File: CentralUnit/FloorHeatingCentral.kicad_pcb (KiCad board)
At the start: 2 copper layers, 100 x 100 mm, 118 parts, among them J1 Conn_01x02, J10 Conn_01x02, J11 Conn_01x02, J12 Conn_01x02, J13 Conn_01x02, J14 Conn_01x02, J15 Conn_01x03, J16 Conn_01x03, J17 Conn_01x03, J18 Conn_01x03, J19 Conn_01x03, J2 Conn_01x03, J20 Conn_01x03, J21 Conn_01x03, J22 Conn_01x03, J23 Conn_01x03, J24 Conn_01x03, J25 Conn_02x05_Odd_Even, J26 Conn_01x02, J3 Conn_01x20, J4 Conn_01x06, J5 Conn_01x02, J6 Conn_01x02, J7 Conn_01x02, J8 Conn_01x02, J9 Conn_01x02, Q1 Q_NMOS_GDS, Q10 Q_NMOS_GDS, Q2 Q_NMOS_GDS, Q3 Q_NMOS_GDS, Q4 Q_NMOS_GDS, Q5 Q_NMOS_GDS, Q6 Q_NMOS_GDS, Q7 Q_NMOS_GDS, Q8 Q_NMOS_GDS, Q9 Q_NMOS_GDS, U1 ESP32-WROOM, U10 LM1117-3.3, U2 ISO1540DR, U3 ISO1540DR, U4 ISO1540DR, U5 ISO1540DR, U6 ISO1540DR, U7 74HC595D_118, U8 74HC595D_118, U9 MP1584

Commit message: Added alternative resistor to connect LCD brightness to DAC
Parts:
- added R51: R, Resistors_SMD:R_0603, F.Cu at (169.5, 126.5)
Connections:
- net /ActuatorConn/GATE renamed /GATE_3
- net /sheet5C0162C8/GATE renamed /GATE_9
- net /sheet5C0163D9/GATE renamed /GATE
- net /sheet5C0163DC/GATE renamed /GATE_8
- net /sheet5C016537/GATE renamed /GATE_7
- net /sheet5C01653A/GATE renamed /GATE_6
- net /sheet5C01653D/GATE renamed /GATE_5
- net /sheet5C016540/GATE renamed /GATE_4
- net /sheet5C0169FB/GATE renamed /GATE_2
- net /sheet5C0169FE/GATE renamed /GATE_1
- net Net-(R3-Pad2) renamed /TXD
- net Net-(R4-Pad2) renamed /RXD
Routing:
- net /IO0: track 34.2 -> 92.1 mm
- net Net-(J3-Pad3): track 6.59 -> 21.3 mm, vias 0 -> 1

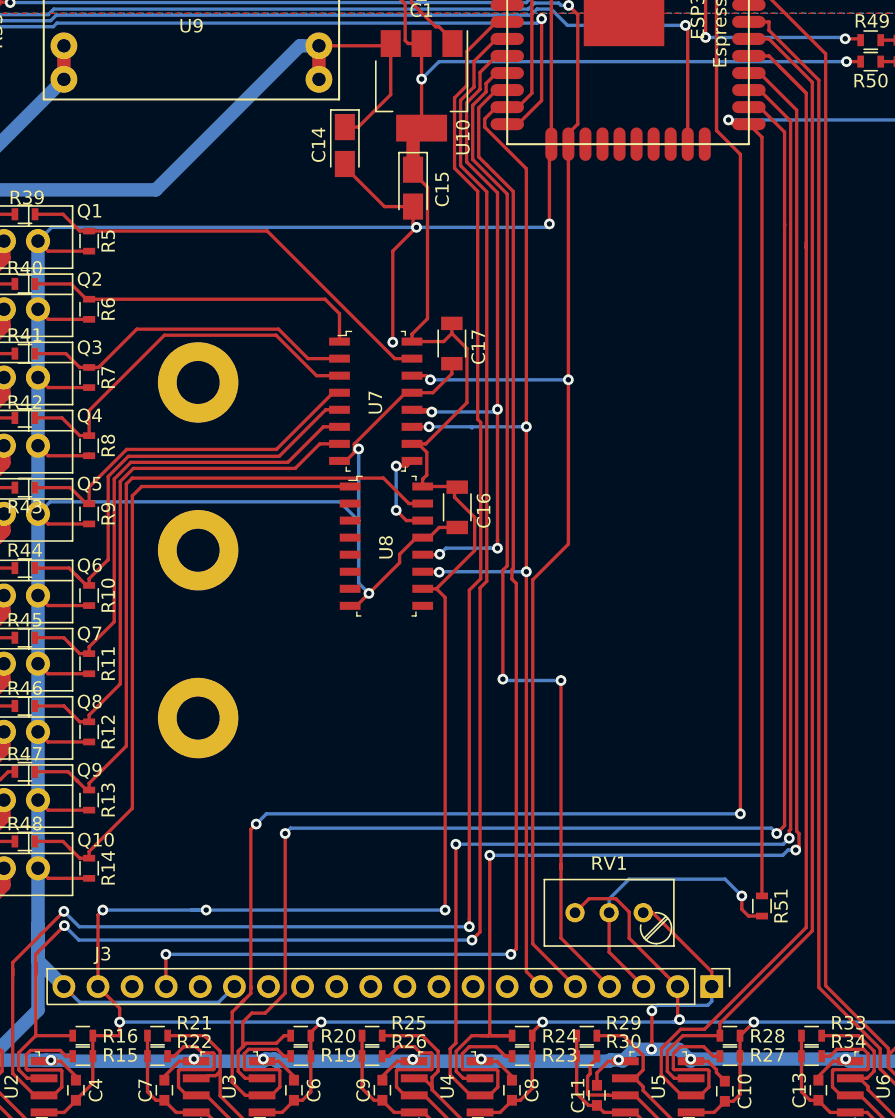
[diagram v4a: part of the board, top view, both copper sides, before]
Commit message: Added possibility to PWM LCD light and updated README
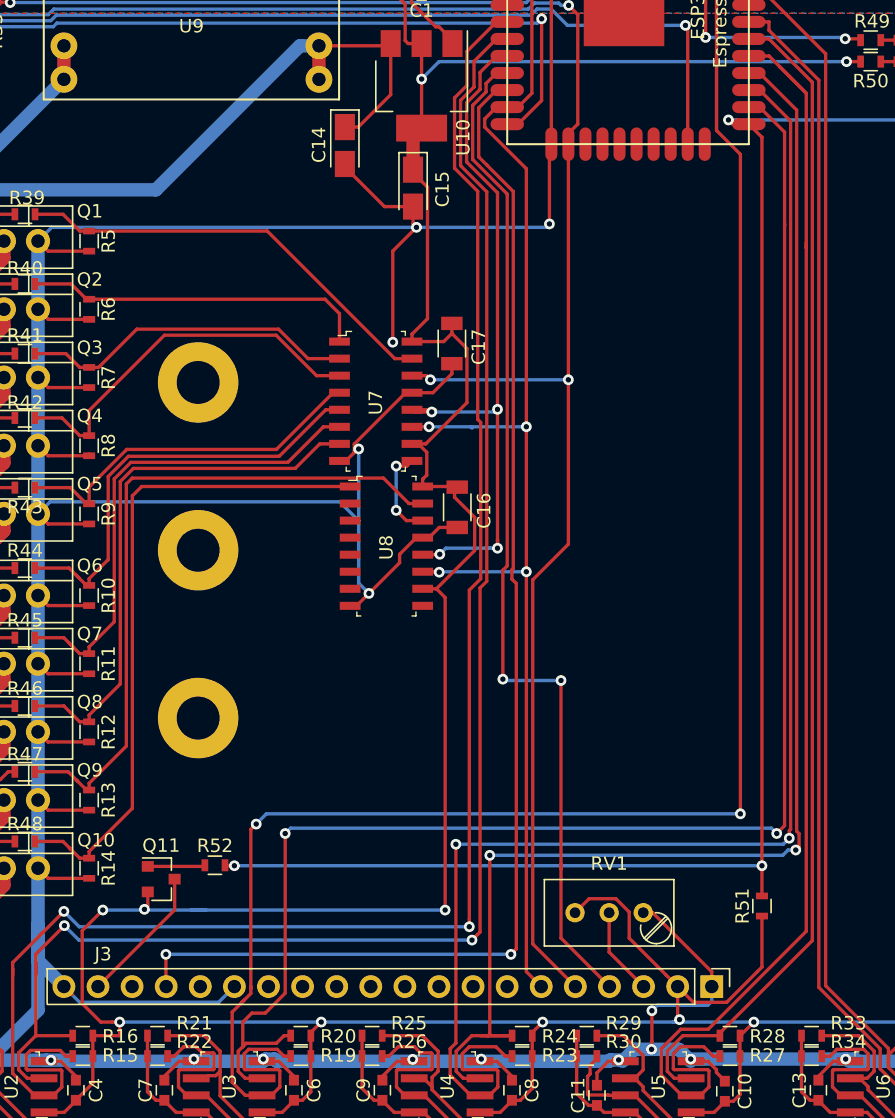
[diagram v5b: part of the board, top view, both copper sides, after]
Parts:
- added Q11: Q_PMOS_GSD, TO_SOT_Packages_SMD:SOT-23, F.Cu at (124.8, 124.5)
- added R52: 330, Resistors_SMD:R_0603, F.Cu at (128.8, 123.5)
- R51: value R -> Inf
- turned R51 to 90 degrees
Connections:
- J3 pad 19: +3V3 -> /VDD_DL
- R51 pad 1: /IO0 -> +3V3
- R51 pad 2: Net-(J3-Pad3) -> /IO0
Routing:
- net /IO0: track 92.1 -> 132.1 mm, vias 1 -> 3
- net +3V3: track 331.7 -> 346.5 mm
- net Net-(J3-Pad3): track 21.3 -> 6.59 mm, vias 1 -> 0
- net /VDD_DL: track 0.00 -> 10.4 mm
- net Net-(Q11-Pad1): track 0.00 -> 4.29 mm

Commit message: Major work changing over to 868MHz solution. Current state unfinished
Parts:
- removed C10, C11, C12, C13, C5, C6, C7, C8, C9: 0.1u, Capacitors_SMD:C_0603
- removed C14, C15: 10u, Capacitors_Tantalum_SMD:CP_Tantalum_Case-A_EIA-3216-18_Reflow
- removed C16, C17: 0.1u, Capacitors_SMD:C_1206
- removed D2: LED, LEDs:LED_0603
- removed J14: Conn_01x02, parts:ScrewTerminal_2x2.54
- removed J15, J16, J17, J18, J19, J20, J21, J22, J23, J24: Conn_01x03, parts:ScrewTerminal_3x2.54
- removed J25: Conn_02x05_Odd_Even, Pin_Headers:Pin_Header_Straight_2x05_Pitch2.54mm
- removed J26: Conn_01x02, Pin_Headers:Pin_Header_Straight_1x02_Pitch2.54mm
- removed R28, R31, R32: 2.7K, Resistors_SMD:R_0603
- removed R29, R30, R33, R34: 300R, Resistors_SMD:R_0603
- removed R35, R36, R37, R38: 100R, Resistors_SMD:R_0603
- removed R39, R40, R41, R42, R43, R44, R45, R46, R47, R48: 560R, Resistors_SMD:R_0603
- removed R49, R50: 660R, Resistors_SMD:R_0603
- removed R51: Inf, Resistors_SMD:R_0603
- removed R52: 330, Resistors_SMD:R_0603
- removed U10: LM1117-3.3, TO_SOT_Packages_SMD:SOT-223-3_TabPin2
- removed U7, U8: 74HC595D_118, digikey-footprints:SOIC-16_W3.90mm
- removed U9: MP1584, mp1584:MP1584
- added JP1: Jumper_2_Open, TestPoint:TestPoint_2Pads_Pitch2.54mm_Drill0.8mm, F.Cu at (96.0, 109.5)
- C1: footprint Capacitors_SMD:C_0603 -> Capacitor_SMD:C_1206_3216Metric
- C2: value 10u -> 0.1u; footprint Capacitors_Tantalum_SMD:CP_Tantalum_Case-A_EIA-3216-18_Reflow -> Capacitor_SMD:C_1206_3216Metric
- C3, C4: value 0.1u -> 10u; footprint Capacitors_SMD:C_0603 -> Capacitor_Tantalum_SMD:CP_EIA-3216-18_Kemet-A
- D1: footprint LEDs:LED_0603 -> LED_SMD:LED_0603_1608Metric
- H1, H2: moved to F.Cu
- J1: value Conn_01x02 -> Screw_Terminal_01x02; footprint Pin_Headers:Pin_Header_Straight_1x02_Pitch2.54mm -> TerminalBlock_Phoenix:TerminalBlock_Phoenix_MKDS-3-2-5.08_1x02_P5.08mm_Horizontal
- J10, J11, J12, J13, J5, J6, J7, J8, J9: value Conn_01x02 -> Screw_Terminal_01x02; footprint parts:ScrewTerminal_2x2.54 -> TerminalBlock_Phoenix:TerminalBlock_Phoenix_MKDS-3-2-5.08_1x02_P5.08mm_Horizontal
- J2: value Conn_01x03 -> Conn_02x05_Odd_Even; footprint Pin_Headers:Pin_Header_Straight_1x03_Pitch2.54mm -> Connector_IDC:IDC-Header_2x05_P2.54mm_Vertical
- J4: value Conn_01x06 -> Screw_Terminal_01x02; footprint Pin_Headers:Pin_Header_Straight_1x06_Pitch2.54mm -> TerminalBlock_Phoenix:TerminalBlock_Phoenix_MKDS-3-2-5.08_1x02_P5.08mm_Horizontal
- Q1, Q10, Q2, Q3, Q4, Q5, Q6, Q7, Q8, Q9: footprint TO_SOT_Packages_THT:TO-220-3_Vertical -> Package_TO_SOT_THT:TO-220-3_Vertical
- Q11: value Q_PMOS_GSD -> Q_NMOS_GDS; footprint TO_SOT_Packages_SMD:SOT-23 -> Package_TO_SOT_THT:TO-220-3_Vertical
- R1, R11, R13, R9: footprint Resistors_SMD:R_0603 -> Resistor_SMD:R_1206_3216Metric
- R10, R12, R14, R8: value 10K -> 560R; footprint Resistors_SMD:R_0603 -> Resistor_SMD:R_1206_3216Metric
- R15, R19, R23, R27: value 2.7K -> 10K; footprint Resistors_SMD:R_0603 -> Resistor_SMD:R_1206_3216Metric
- R16, R20, R24: value 2.7K -> 560R; footprint Resistors_SMD:R_0603 -> Resistor_SMD:R_1206_3216Metric
- R17, R21, R25: value 300R -> 10K; footprint Resistors_SMD:R_0603 -> Resistor_SMD:R_1206_3216Metric
- R18, R22, R26: value 300R -> 560R; footprint Resistors_SMD:R_0603 -> Resistor_SMD:R_1206_3216Metric
- R2: value 4.7K -> 560R; footprint Resistors_SMD:R_0603 -> Resistor_SMD:R_1206_3216Metric
- R3, R4: value 470R -> 100R; footprint Resistors_SMD:R_0603 -> Resistor_SMD:R_0201_0603Metric
- R5, R7: value 10K -> 100R; footprint Resistors_SMD:R_0603 -> Resistor_SMD:R_0201_0603Metric
- R6: value 10K -> 660R; footprint Resistors_SMD:R_0603 -> Resistor_SMD:R_1206_3216Metric
- RV1: footprint Potentiometers:Potentiometer_Trimmer_Bourns_3296W -> Potentiometer_SMD:Potentiometer_Bourns_3269W_Vertical
- U1: value ESP32-WROOM -> ESP32-DevKitC; footprint ESP32-footprints-Lib:ESP32-WROOM -> Espressif:ESP32-DevKitC
- U2, U3: value ISO1540DR -> 74HC595D_118; footprint digikey-footprints:SOIC-8_W3.9mm -> digikey-footprints:SOIC-16_W3.90mm
- U4: value ISO1540DR -> RFM69-ATSHA-breakout; footprint digikey-footprints:SOIC-8_W3.9mm -> RFM69HCW_ATSHA204A_Breakout:RFM69HCW_ATSHA204A_Breakout
- U5: value ISO1540DR -> MP1584; footprint digikey-footprints:SOIC-8_W3.9mm -> mp1584:MP1584
- U6: value ISO1540DR -> LM1117-5.0; footprint digikey-footprints:SOIC-8_W3.9mm -> Package_TO_SOT_SMD:SOT-223-3_TabPin2
- moved H1 284.1 mm to (388.4, 212.4)
- moved H2 237.8 mm to (399.6, 212.4)
- moved J4 140.6 mm to (96.3, 164.1), turned to 0 degrees
- moved R2 117.4 mm to (111.8, 132.1)
- moved J2 116.1 mm to (93.5, 117.5), turned to 0 degrees
- moved R4 108.0 mm to (100.6, 120.4), turned to 180 degrees
- moved R3 104.5 mm to (100.6, 117.9), turned to 180 degrees
- moved J1 101.5 mm to (96.5, 92.1), turned to 90 degrees
- moved J13 95.1 mm to (187.7, 164.1), turned to 0 degrees
- moved J12 89.1 mm to (177.6, 164.1), turned to 0 degrees
- moved D1 87.7 mm to (94.0, 76.5), turned to 0 degrees
- moved J5 87.1 mm to (106.4, 164.1), turned to 0 degrees
- moved R1 86.7 mm to (111.8, 137.2), turned to -90 degrees
- moved J11 84.2 mm to (167.4, 164.1), turned to 0 degrees
- moved J6 83.0 mm to (116.6, 164.1), turned to 0 degrees
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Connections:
- C1 pad 1: Net-(C1-Pad1) -> GND
- C1 pad 2: GND -> +3V3
- C2 pad 1: +3V3 -> GND
- C2 pad 2: GND -> +3V3
- C3 pad 1: +3V3 -> +7.5V
- C4 pad 1: +3V3 -> +5V
- J1 pad 1: Net-(C1-Pad1) -> +24V
- J10 pad 1: Net-(J10-Pad1) -> /sheet5C01653D/ValSW
- J11 pad 1: Net-(J11-Pad1) -> /sheet5C016540/ValSW
- J12 pad 1: Net-(J12-Pad1) -> /sheet5C0169FB/ValSW
- J13 pad 1: Net-(J13-Pad1) -> /sheet5C0169FE/ValSW
- J2 pad 1: (no net) -> Net-(J2-Pad1)
- J2 pad 2: /IO0 -> Net-(J2-Pad2)
- J2 pad 3: Net-(J2-Pad3) -> GND
- J3 pad 10: (no net) -> unconnected-(J3-Pad10)
- J3 pad 11: (no net) -> unconnected-(J3-Pad11)
- J3 pad 12: (no net) -> unconnected-(J3-Pad12)
- J3 pad 13: (no net) -> unconnected-(J3-Pad13)
- J3 pad 14: (no net) -> unconnected-(J3-Pad14)
- J3 pad 16: (no net) -> unconnected-(J3-Pad16)
- J3 pad 18: (no net) -> unconnected-(J3-Pad18)
- J3 pad 19: /VDD_DL -> +3V3
- J3 pad 20: GND -> /GND_DL_SW
- J3 pad 5: /HSPI_MOSI_IO13 -> /VSPI_MOSI
- J3 pad 6: /HSPI_CLK_IO14 -> /VSPI_CLK
- J3 pad 7: (no net) -> unconnected-(J3-Pad7)
- J3 pad 8: (no net) -> unconnected-(J3-Pad8)
- J3 pad 9: (no net) -> unconnected-(J3-Pad9)
- J4 pad 1: GND -> /ActuatorConn/ValSW
- J4 pad 2: Net-(J4-Pad2) -> +24V
- J5 pad 1: Net-(J5-Pad1) -> /sheet5C0162C8/ValSW
- J6 pad 1: Net-(J6-Pad1) -> /sheet5C0163D9/ValSW
- J7 pad 1: Net-(J7-Pad1) -> /sheet5C0163DC/ValSW
- J8 pad 1: Net-(J8-Pad1) -> /sheet5C016537/ValSW
- J9 pad 1: Net-(J9-Pad1) -> /sheet5C01653A/ValSW
- Q1 pad 2: Net-(J5-Pad1) -> /GND_DL_SW
- Q10 pad 2: Net-(J14-Pad1) -> /sheet5C0169FB/ValSW
- Q11 pad 2: +3V3 -> /sheet5C0169FE/ValSW
- Q11 pad 3: /VDD_DL -> GND
- Q2 pad 2: Net-(J6-Pad1) -> /ActuatorConn/ValSW
- Q3 pad 2: Net-(J7-Pad1) -> /sheet5C0162C8/ValSW
- Q4 pad 2: Net-(J8-Pad1) -> /sheet5C0163D9/ValSW
- Q5 pad 2: Net-(J9-Pad1) -> /sheet5C0163DC/ValSW
- Q6 pad 2: Net-(J10-Pad1) -> /sheet5C016537/ValSW
- Q7 pad 2: Net-(J11-Pad1) -> /sheet5C01653A/ValSW
- Q8 pad 2: Net-(J12-Pad1) -> /sheet5C01653D/ValSW
- Q9 pad 2: Net-(J13-Pad1) -> /sheet5C016540/ValSW
- R1 pad 1: Net-(C1-Pad1) -> /DL_SW
- R1 pad 2: +3V3 -> GND
- R10 pad 1: /GATE_6 -> /sheet5C0162C8/GATE
- R10 pad 2: GND -> Net-(Q3-Pad1)
- R11 pad 1: /GATE_5 -> /sheet5C0162C8/GATE
- R12 pad 1: /GATE_4 -> /sheet5C0163D9/GATE
- R12 pad 2: GND -> Net-(Q4-Pad1)
- R13 pad 1: /GATE_2 -> /sheet5C0163D9/GATE
- R14 pad 1: /GATE_1 -> /sheet5C0163DC/GATE
- R14 pad 2: GND -> Net-(Q5-Pad1)
- R15 pad 1: +3V3 -> /sheet5C0163DC/GATE
- R15 pad 2: /INP0 -> GND
- R16 pad 1: /INP1 -> /sheet5C016537/GATE
- R16 pad 2: +3V3 -> Net-(Q6-Pad1)
- R17 pad 1: +5V -> /sheet5C016537/GATE
- R17 pad 2: Net-(J15-Pad3) -> GND
- R18 pad 1: Net-(J16-Pad3) -> /sheet5C01653A/GATE
- R18 pad 2: +5V -> Net-(Q7-Pad1)
- R19 pad 1: +3V3 -> /sheet5C01653A/GATE
- R19 pad 2: /INP2 -> GND
- R2 pad 1: GND -> /DL_SW
- R2 pad 2: Net-(J2-Pad3) -> Net-(Q1-Pad1)
- R20 pad 1: /INP3 -> /sheet5C01653D/GATE
- R20 pad 2: +3V3 -> Net-(Q8-Pad1)
- R21 pad 1: +5V -> /sheet5C01653D/GATE
- R21 pad 2: Net-(J17-Pad3) -> GND
- R22 pad 1: Net-(J18-Pad3) -> /sheet5C016540/GATE
- R22 pad 2: +5V -> Net-(Q9-Pad1)
- R23 pad 1: +3V3 -> /sheet5C016540/GATE
- R23 pad 2: /INP4 -> GND
- R24 pad 1: /INP5 -> /sheet5C0169FB/GATE
- R24 pad 2: +3V3 -> Net-(Q10-Pad1)
- R25 pad 1: +5V -> /sheet5C0169FB/GATE
- R25 pad 2: Net-(J19-Pad3) -> GND
- R26 pad 1: Net-(J20-Pad3) -> /sheet5C0169FE/GATE
- R26 pad 2: +5V -> Net-(Q11-Pad1)
- R27 pad 1: +3V3 -> /sheet5C0169FE/GATE
- R27 pad 2: /INP6 -> GND
- R3 pad 1: Net-(J4-Pad2) -> /TMS
- R3 pad 2: /TXD -> Net-(J2-Pad2)
- R4 pad 1: Net-(J4-Pad3) -> /TCK
- R4 pad 2: /RXD -> Net-(J2-Pad4)
- R5 pad 1: /GATE_3 -> /TDO
- R5 pad 2: GND -> Net-(J2-Pad6)
- R6 pad 1: /GATE_9 -> Net-(D1-Pad2)
- R6 pad 2: GND -> /LED
- R7 pad 1: /GATE -> /TDI
- R7 pad 2: GND -> Net-(J2-Pad8)
- R8 pad 1: /GATE_8 -> /ActuatorConn/GATE
- R8 pad 2: GND -> Net-(Q2-Pad1)
- R9 pad 1: /GATE_7 -> /ActuatorConn/GATE
- U1 pad 1: GND -> +3V3
- U1 pad 10: /SR_LATCH -> /DISP_CS
- U1 pad 11: /DISP_CS -> /DISP_RST
- U1 pad 12: /DISP_RST -> /TMS
- U1 pad 13: /HSPI_CLK_IO14 -> /TDI
- U1 pad 14: /HSPI_MISO_IO12 -> GND
- U1 pad 15: GND -> /TCK
- U1 pad 16: /HSPI_MOSI_IO13 -> unconnected-(U1-Pad16)
- U1 pad 17: (no net) -> unconnected-(U1-Pad17)
- U1 pad 18: (no net) -> unconnected-(U1-Pad18)
- U1 pad 19: (no net) -> +5V
- U1 pad 2: +3V3 -> unconnected-(U1-Pad2)
- U1 pad 20: (no net) -> unconnected-(U1-Pad20)
- U1 pad 21: (no net) -> unconnected-(U1-Pad21)
- U1 pad 22: (no net) -> unconnected-(U1-Pad22)
- U1 pad 23: /HSPI_CS0_IO15 -> /TDO
- U1 pad 24: (no net) -> unconnected-(U1-Pad24)
- U1 pad 25: /IO0 -> unconnected-(U1-Pad25)
- U1 pad 26: /INP3 -> /DL_SW
- U1 pad 27: /INP4 -> /RFM69_IRQ
- U1 pad 28: /INP5 -> /RFM69_RST
- U1 pad 29: /INP6 -> /RFM69_CS
- U1 pad 3: Net-(C1-Pad1) -> unconnected-(U1-Pad3)
- U1 pad 30: /INP7 -> /VSPI_SCK
- U1 pad 31: /INP8 -> /VSPI_MISO
- U1 pad 32: (no net) -> GND
- U1 pad 33: /INP9 -> unconnected-(U1-Pad33)
- U1 pad 34: /RXD -> unconnected-(U1-Pad34)
- U1 pad 35: /TXD -> unconnected-(U1-Pad35)
- U1 pad 36: /INP2 -> unconnected-(U1-Pad36)
- U1 pad 37: /LED -> /VSPI_MOSI
- U1 pad 4: (no net) -> unconnected-(U1-Pad4)
- U1 pad 5: (no net) -> unconnected-(U1-Pad5)
- U1 pad 6: (no net) -> unconnected-(U1-Pad6)
- U1 pad 7: (no net) -> /LED
- U1 pad 8: /INP0 -> unconnected-(U1-Pad8)
- U1 pad 9: /INP1 -> /SR_LATCH
- U2 pad 1: +3V3 -> /sheet5C0162C8/GATE
- U2 pad 2: /INP0 -> /sheet5C0163D9/GATE
- U2 pad 3: /INP1 -> /sheet5C0163DC/GATE
- U2 pad 4: GND -> /sheet5C016537/GATE
- U2 pad 5: GND -> /sheet5C01653A/GATE
- U2 pad 6: Net-(J16-Pad3) -> /sheet5C01653D/GATE
- U2 pad 7: Net-(J15-Pad3) -> /sheet5C016540/GATE
- U2 pad 8: +5V -> GND
- U3 pad 1: +3V3 -> /sheet5C0169FE/GATE
- U3 pad 2: /INP2 -> unconnected-(U3-Pad2)
- U3 pad 3: /INP3 -> unconnected-(U3-Pad3)
- U3 pad 4: GND -> unconnected-(U3-Pad4)
- U3 pad 5: GND -> unconnected-(U3-Pad5)
- U3 pad 6: Net-(J18-Pad3) -> unconnected-(U3-Pad6)
- U3 pad 7: Net-(J17-Pad3) -> unconnected-(U3-Pad7)
- U3 pad 8: +5V -> GND
- U4 pad 1: +3V3 -> /RFM69_RST
- U4 pad 2: /INP4 -> /RFM69_IRQ
- U4 pad 3: /INP5 -> unconnected-(U4-Pad3)
- U4 pad 4: GND -> unconnected-(U4-Pad4)
- U4 pad 5: GND -> unconnected-(U4-Pad5)
- U4 pad 6: Net-(J20-Pad3) -> unconnected-(U4-Pad6)
- U4 pad 7: Net-(J19-Pad3) -> unconnected-(U4-Pad7)
- U4 pad 8: +5V -> +3V3
- U5 pad 1: +3V3 -> +24V
- U5 pad 2: /INP6 -> GND
- U5 pad 3: /INP7 -> +7.5V
- U6 pad 1: +3V3 -> GND
- U6 pad 2: /INP8 -> +5V
- U6 pad 3: /INP9 -> +7.5V
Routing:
- net +5V: track 294.2 -> 33.0 mm, vias 1 -> 0
- net GND: track 632.5 -> 451.2 mm, vias 19 -> 6
- net +24V: track 125.3 -> 281.4 mm
- net /INP2: track 138.5 -> 0.00 mm, vias 2 -> 0
- net /HSPI_CLK_IO14: track 135.4 -> 0.00 mm, vias 6 -> 0
- net /HSPI_MOSI_IO13: track 133.9 -> 0.00 mm, vias 4 -> 0
- net /IO0: track 132.1 -> 0.00 mm, vias 3 -> 0
- net /INP0: track 129.1 -> 0.00 mm, vias 2 -> 0
- net /VSPI_MOSI: track 0.00 -> 121.9 mm, vias 0 -> 1
- net /INP1: track 119.1 -> 0.00 mm, vias 2 -> 0
- net /INP3: track 118.6 -> 0.00 mm, vias 2 -> 0
- net /INP4: track 113.6 -> 0.00 mm, vias 2 -> 0
- net /INP5: track 106.9 -> 0.00 mm, vias 2 -> 0
- net /INP6: track 101.5 -> 0.00 mm
- net /INP8: track 97.2 -> 0.00 mm
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- removed copper zone on B.Cu, net GND
- removed copper zone on F.Cu, net GND
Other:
- board size 100 x 100 mm -> 110 x 110 mm
- net class 24V removed
- net class Default removed
- board text removed: "EN"
- board text removed: "FLASH↦"

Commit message: More cleanup and potentially final routing
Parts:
- H1, H2, R3, R4, R5, R7: moved to B.Cu
- U2, U3: footprint digikey-footprints:SOIC-16_W3.90mm -> Package_SO:SOIC-16_3.9x9.9mm_P1.27mm
- moved H1 293.2 mm to (114.0, 109.2), turned to 180 degrees
- moved H2 234.5 mm to (189.0, 109.2), turned to 180 degrees
- moved C3 29.5 mm to (115.3, 67.0), turned to 0 degrees
- moved C4 21.2 mm to (120.4, 72.8), turned to 90 degrees
- moved U5 18.2 mm to (116.0, 71.5), turned to -90 degrees
- moved U6 18.1 mm to (115.3, 72.8), turned to -90 degrees
- moved J1 5.21 mm to (96.5, 86.9), turned to -90 degrees
- turned RV1 to 0 degrees
- turned U2 to 90 degrees
- turned U3 to -90 degrees
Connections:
- J1 pad 1: +24V -> GND
- J1 pad 2: GND -> +24V
- U1 pad 24: unconnected-(U1-Pad24) -> /DL_SW
- U1 pad 26: /DL_SW -> /ATSHA
- U2 pad 9: unconnected-(U2-Pad9) -> Net-(U2-Pad9)
- U3 pad 14: unconnected-(U3-Pad14) -> Net-(U2-Pad9)
- U4 pad 16: unconnected-(U4-Pad16) -> /ATSHA
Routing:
- net /DL_SW: track 41.7 -> 77.9 mm, vias 1 -> 2
- net +24V: track 281.4 -> 315.0 mm
- net +5V: track 33.0 -> 49.6 mm
- net Net-(U2-Pad9): track 0.00 -> 15.3 mm, vias 0 -> 2
- net /TMS: track 51.0 -> 63.1 mm
- net /DISP_RST: track 57.9 -> 69.9 mm, vias 0 -> 3
- net /TCK: track 46.7 -> 58.5 mm, vias 1 -> 2
- net /ATSHA: track 0.00 -> 11.7 mm
- net /TDO: track 70.0 -> 78.9 mm
- net /sheet5C0169FB/GATE: track 43.6 -> 52.2 mm
- net GND: track 451.2 -> 459.7 mm, vias 6 -> 8
- net /LED: track 33.1 -> 41.2 mm, vias 0 -> 2
- net /TDI: track 58.9 -> 66.4 mm, vias 1 -> 2
- net /DISP_CS: track 80.8 -> 86.3 mm, vias 2 -> 3
- net +3V3: track 272.8 -> 277.4 mm, vias 8 -> 7
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- added copper zone on B.Cu, net GND
- added copper zone on F.Cu, net GND

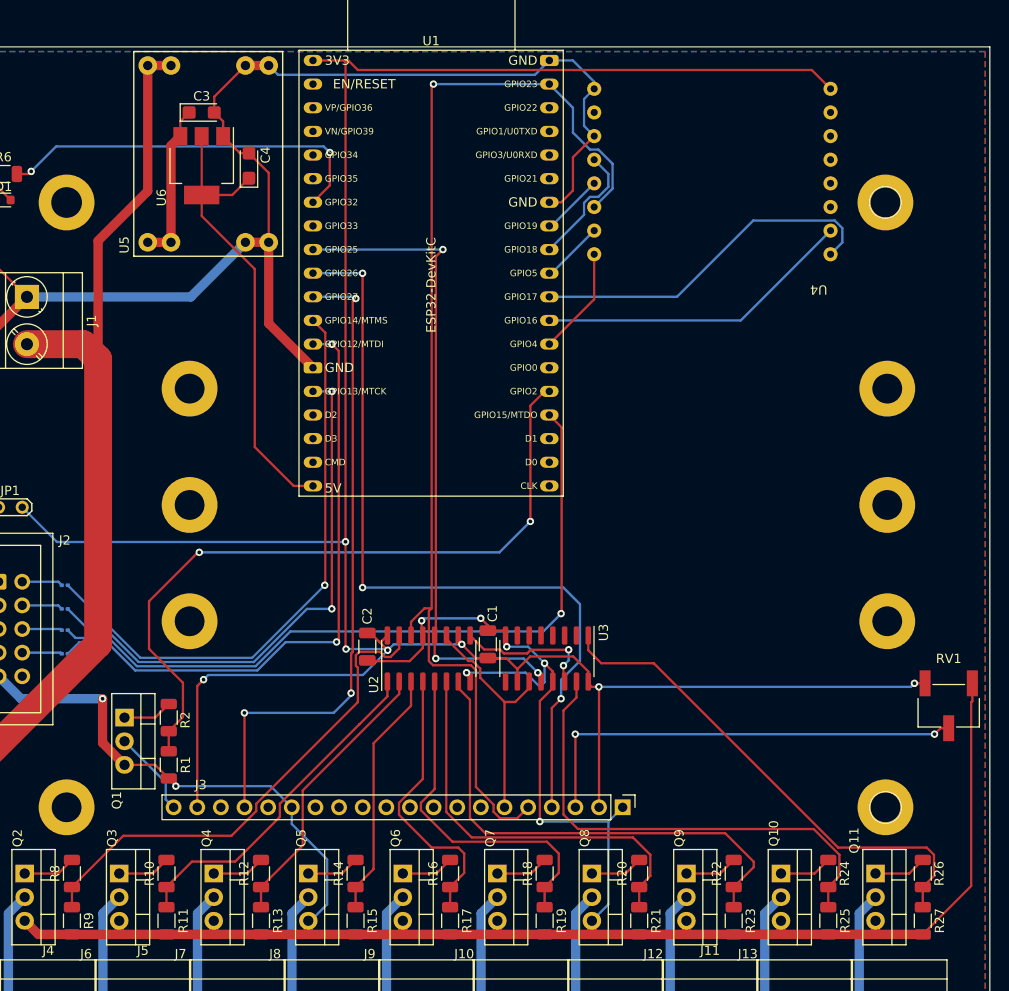
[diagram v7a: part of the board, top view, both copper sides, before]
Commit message: Added power port for thermostats
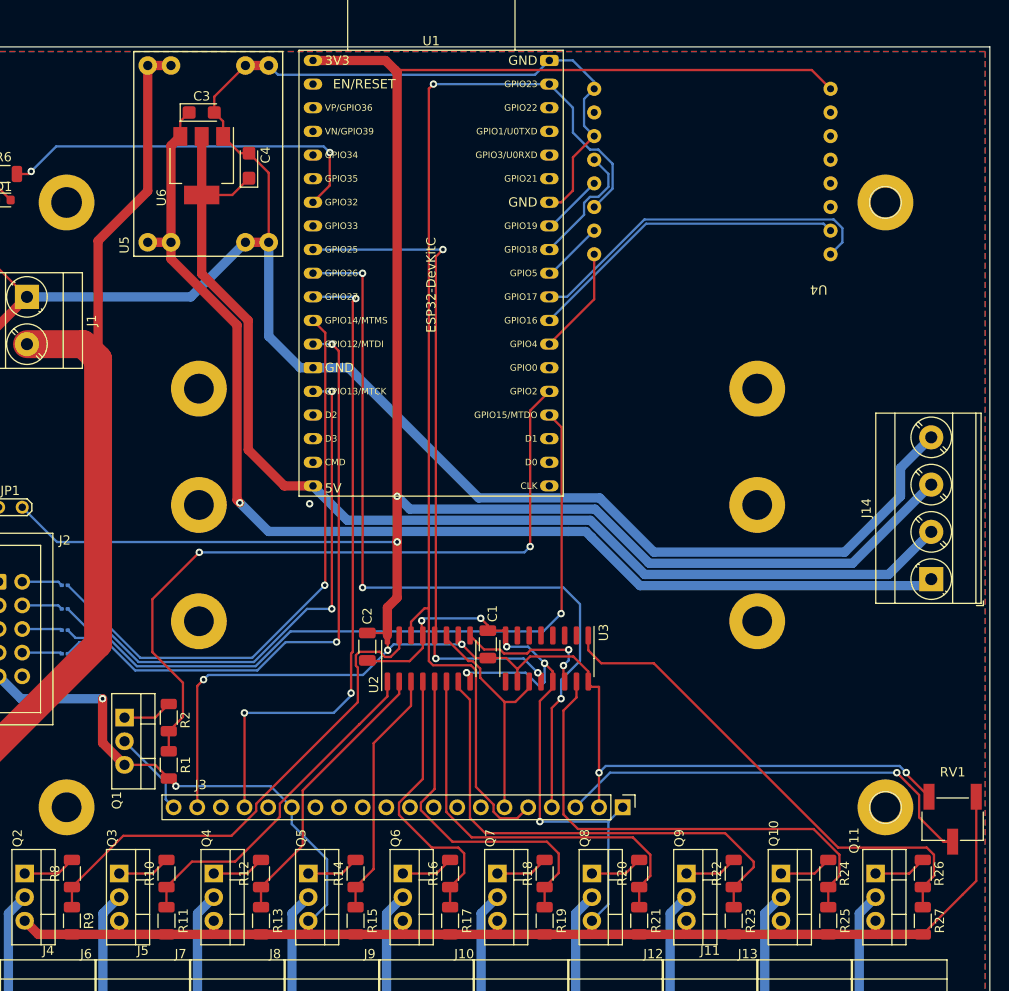
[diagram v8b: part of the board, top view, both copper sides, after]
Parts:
- added J14: Screw_Terminal_01x04, TerminalBlock_Phoenix:TerminalBlock_Phoenix_MKDS-3-4-5.08_1x04_P5.08mm_Horizontal, F.Cu at (193.7, 117.2)
- moved H2 14.0 mm to (175.0, 109.2)
- moved RV1 12.2 mm to (196.0, 143.0)
- moved H1 1.00 mm to (115.0, 109.2)
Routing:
- net +7.5V: track 17.3 -> 126.6 mm, vias 0 -> 2
- net +5V: track 49.6 -> 122.4 mm
- net GND: track 459.7 -> 530.0 mm
- net +3V3: track 277.4 -> 346.3 mm
- net /DL_SW: track 77.9 -> 78.8 mm
- net Net-(J3-Pad3): track 48.3 -> 47.4 mm, vias 2 -> 1
- net /RFM69_IRQ: track 34.2 -> 34.8 mm
